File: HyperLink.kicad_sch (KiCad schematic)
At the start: 45 parts, among them J1 USB_C_Receptacle_USB2.0, J2 Conn_02x05_Odd_Even, J3 Conn_02x05_Odd_Even, SW1 SW_Push, U1 ESP32-C3, U2 PESD2USB5UXT, U3 MIC5504-3.3YM5, Y1 ABM11W-40.0000MHZ-8-B1U-T3

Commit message: Fix matching network component values
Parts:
- C1: value 4p -> 4p5
- C14: value 4p7 -> 3p9
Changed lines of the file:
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@@
       (effects (font (size 1.27 1.27)) (justify right))
     )
-    (property "Value" "4p7" (at 162.56 91.44 0)
+    (property "Value" "3p9" (at 162.56 91.44 0)
       (effects (font (size 1.27 1.27)) (justify right))
     )
@@
       (effects (font (size 1.27 1.27)) (justify right))
     )
-    (property "Value" "4p" (at 187.96 91.44 0)
-      (effects (font (size 1.27 1.27)) (justify right))
-    )
+    (property "Value" "4p5" (at 187.96 91.44 0)
+      (effects (font (size 1.27 1.27)) (justify right))
+    )

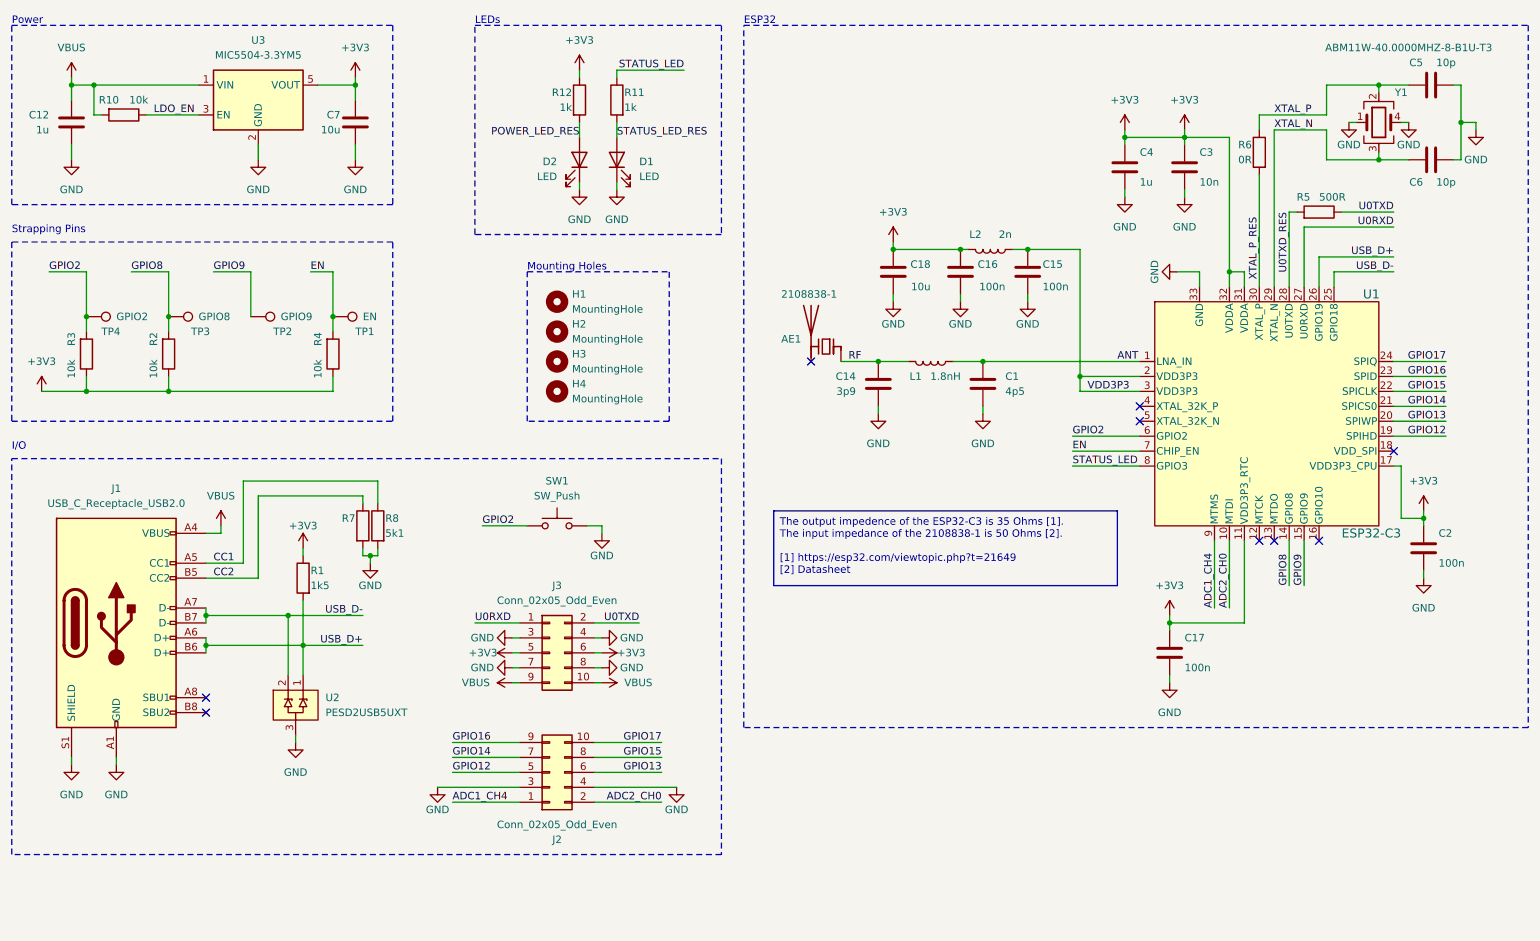
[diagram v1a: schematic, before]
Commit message: Add pulldown resistor to GPIO9 pin
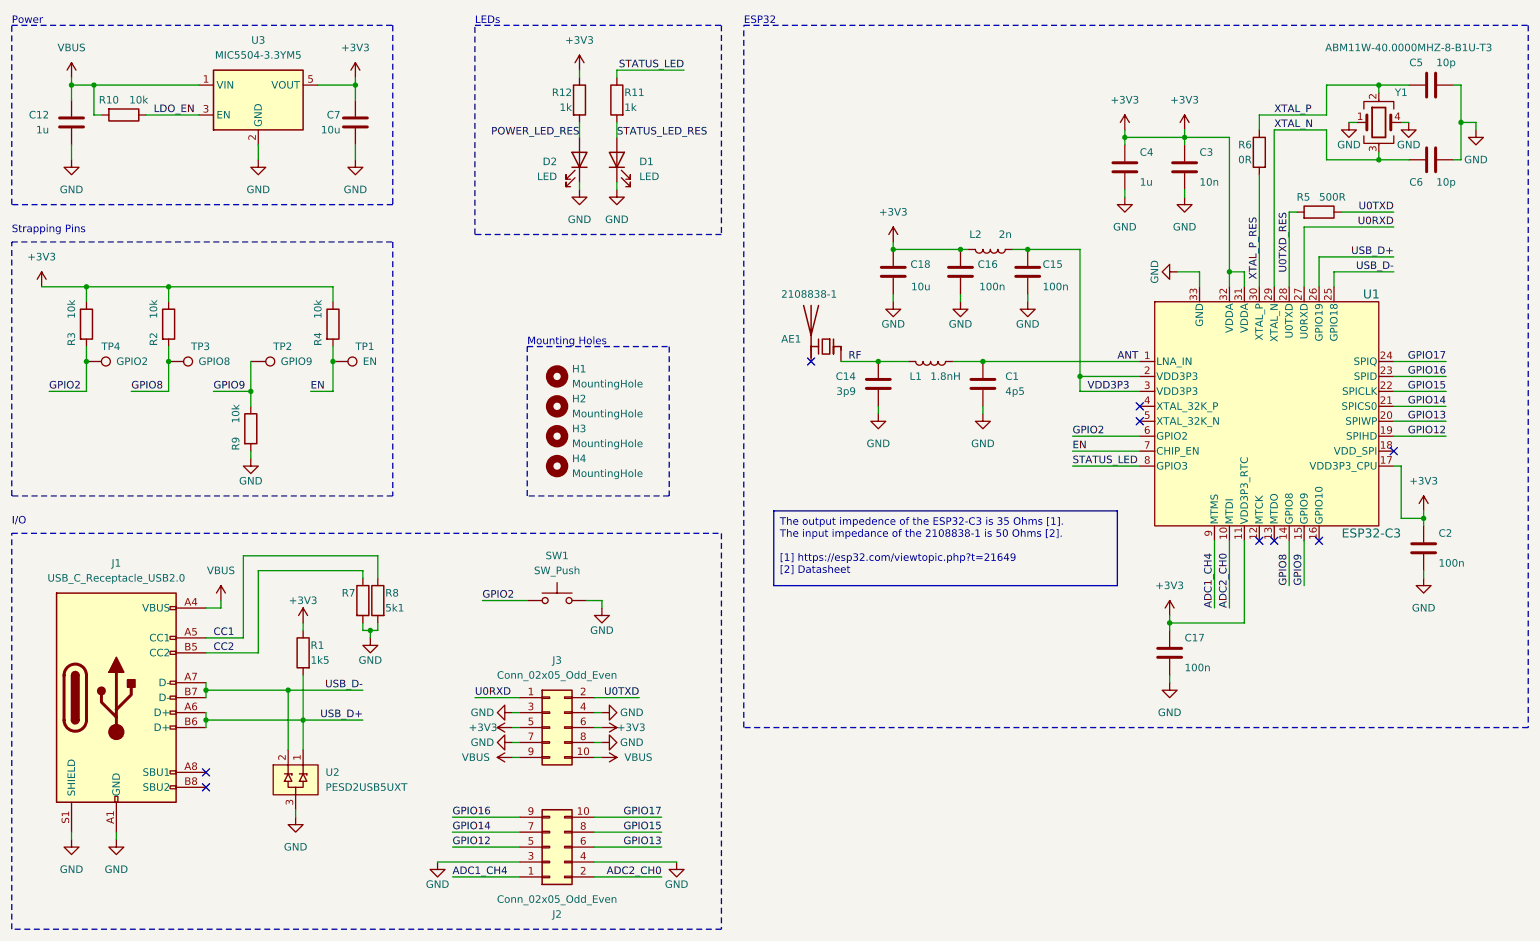
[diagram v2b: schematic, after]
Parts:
- added R9: 10k, Resistor_SMD:R_0402_1005Metric, symbol Device:R
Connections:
- net GND: now also R9.2
- net GPIO9: now also R9.1
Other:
- moved on the sheet: H1, H2, H3, H4, J1, J2, J3, R1, R2, R3, R4, R7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
